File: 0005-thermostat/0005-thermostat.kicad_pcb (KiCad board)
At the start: 2 copper layers, 41 parts, among them J1 EXT_NTC, J2 OUT, J3 PWR, J4 EXT_LED, J5 EXT_P1, J6 EXT_P2, P1 22k, P2 22k, T1 BC847B, T2 BC847B, T3 BC847B

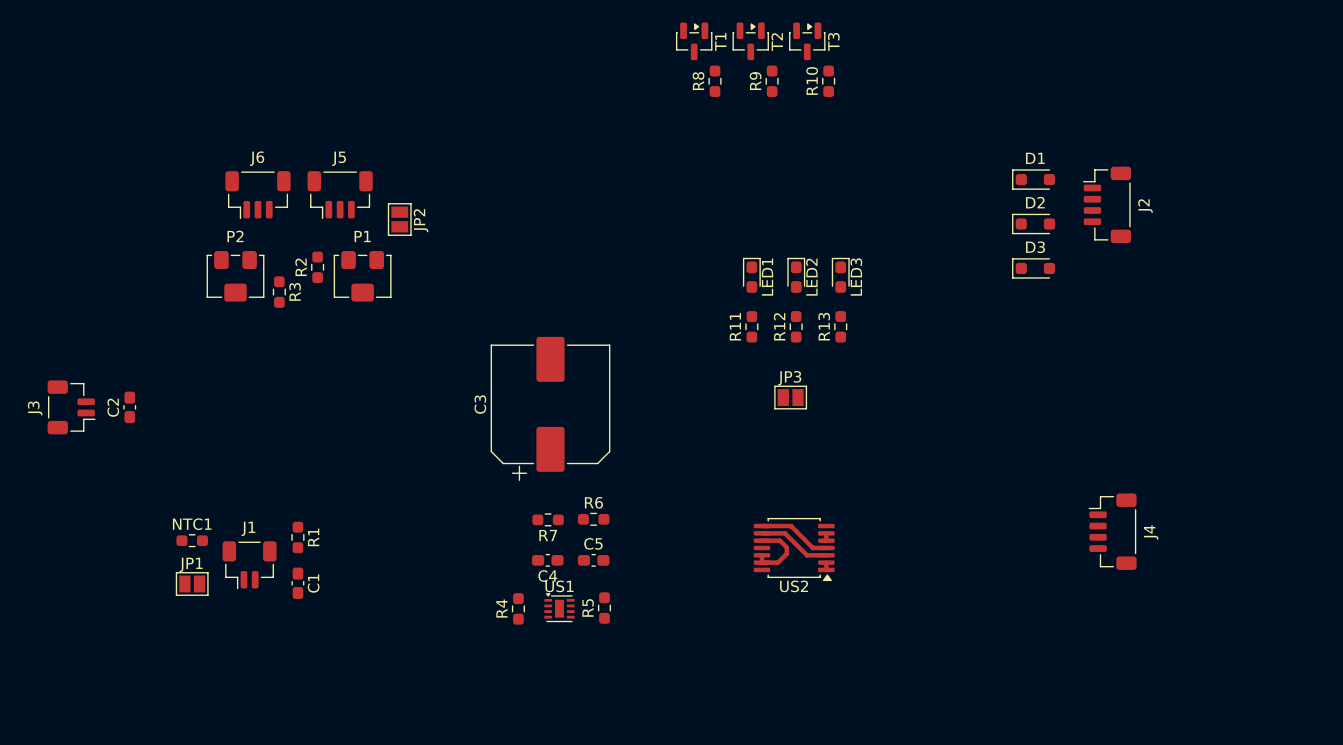
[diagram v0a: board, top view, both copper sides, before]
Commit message: PCB - new sections designed
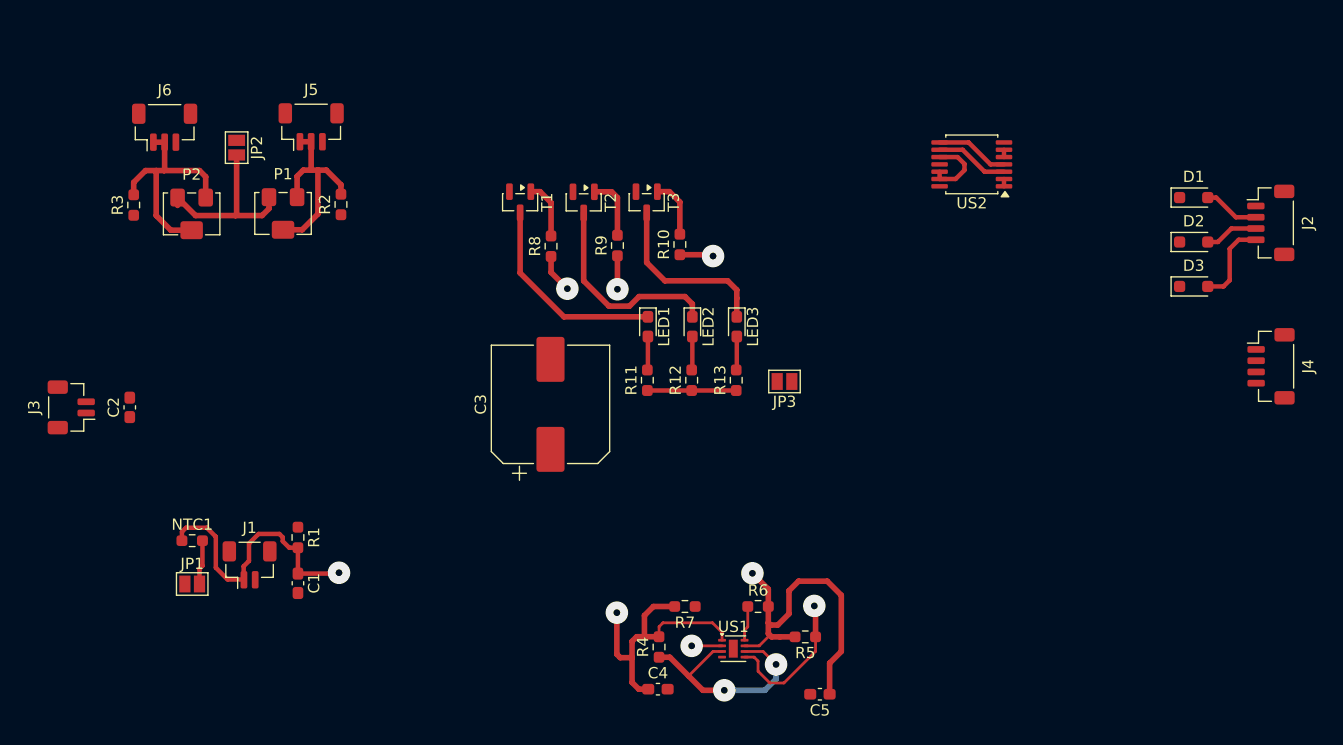
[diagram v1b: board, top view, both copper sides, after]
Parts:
- moved US2 37.6 mm to (177.2, 75.0)
- moved C5 23.4 mm to (163.7, 122.1), turned to 180 degrees
- moved T1 21.1 mm to (137.0, 78.4)
- moved R8 20.7 mm to (139.8, 82.3)
- moved T2 20.6 mm to (142.7, 78.4)
- moved J4 20.3 mm to (203.8, 93.0)
- moved T3 20.2 mm to (148.2, 78.4)
- moved R9 20.1 mm to (145.7, 82.2)
- moved R10 19.6 mm to (151.2, 82.1)
- moved R5 18.0 mm to (162.3, 117.0), turned to 180 degrees
- moved R6 16.5 mm to (158.2, 114.3)
- moved US1 15.9 mm to (155.9, 118.0)
- moved JP2 15.8 mm to (111.8, 73.5)
- moved R3 15.1 mm to (102.7, 78.6), turned to 90 degrees
- moved C4 15.1 mm to (149.2, 121.7), turned to 0 degrees
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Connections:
- J4 pad MP: (no net) -> GNDD
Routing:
- net Net-(J1-Pin_1): track 0.00 -> 45.3 mm, vias 0 -> 3
- net Net-(C5-Pad1): track 0.65 -> 34.3 mm, vias 0 -> 2
- net Net-(J5-Pin_1): track 0.00 -> 31.5 mm, vias 0 -> 1
- net Net-(C4-Pad1): track 0.65 -> 29.3 mm, vias 0 -> 2
- net Net-(J6-Pin_1): track 0.00 -> 23.9 mm, vias 0 -> 1
- net Net-(D3-A): track 0.00 -> 23.0 mm
- net Net-(D1-A): track 0.00 -> 22.9 mm
- net Net-(D2-A): track 0.00 -> 22.7 mm
- net Net-(JP2-B): track 0.00 -> 16.2 mm
- net Net-(JP3-B): track 0.00 -> 7.90 mm
- net Net-(T2-B): track 0.00 -> 5.61 mm
- net Net-(T3-B): track 0.00 -> 5.24 mm
- net Net-(T1-B): track 0.00 -> 5.17 mm
- net Net-(JP1-B): track 0.00 -> 3.96 mm
- net +12V: track 0.00 -> 3.12 mm
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
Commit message: PCB design - connecting modules
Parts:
- moved J3 47.7 mm to (143.8, 106.2), turned to -90 degrees
- moved C2 37.5 mm to (138.6, 106.2), turned to -90 degrees
- moved R3 34.2 mm to (131.6, 96.9)
- moved D3 32.2 mm to (165.7, 93.7)
- moved D1 32.2 mm to (165.7, 85.8)
- moved D2 32.2 mm to (165.7, 89.7)
- moved J2 32.2 mm to (172.5, 88.0)
- moved J4 32.2 mm to (172.5, 100.8)
- moved J6 28.2 mm to (121.2, 95.0), turned to 90 degrees
- moved P2 24.1 mm to (128.7, 91.4), turned to 90 degrees
- moved JP2 19.0 mm to (122.8, 89.1), turned to 0 degrees
- moved NTC1 18.4 mm to (124.3, 100.2), turned to 180 degrees
- moved US2 18.2 mm to (159.8, 80.5), turned to -90 degrees
- moved R1 15.7 mm to (131.7, 102.0)
- moved R2 15.4 mm to (133.7, 87.4)
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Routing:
- net Net-(D2-A): track 22.7 -> 153.5 mm, vias 0 -> 3
- net Net-(D1-A): track 22.9 -> 133.7 mm, vias 0 -> 3
- net Net-(J5-Pin_1): track 31.5 -> 101.3 mm, vias 1 -> 2
- net Net-(D3-A): track 23.0 -> 85.4 mm, vias 0 -> 3
- net Net-(C5-Pad1): track 34.3 -> 83.8 mm, vias 2 -> 3
- net Net-(C4-Pad1): track 29.3 -> 75.1 mm, vias 2 -> 3
- net Net-(J6-Pin_1): track 23.9 -> 59.3 mm, vias 1 -> 2
- net Net-(R9-Pad1): track 2.97 -> 24.2 mm, vias 1 -> 2
- net Net-(J1-Pin_1): track 45.3 -> 61.8 mm
- net Net-(JP3-B): track 7.90 -> 11.9 mm
- net Net-(JP2-B): track 16.2 -> 17.8 mm
- net Net-(JP1-B): track 3.96 -> 5.40 mm

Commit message: PCB finished
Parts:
- added REF**: MountingHole_3.2mm_M3_DIN965_Pad, MountingHole:MountingHole_3.2mm_M3_DIN965_Pad, F.Cu at (177.6, 108.2)
- added REF**: TestPoint_THTPad_D2.0mm_Drill1.0mm, TestPoint:TestPoint_THTPad_D2.0mm_Drill1.0mm, F.Cu at (117.7, 89.2)
- added REF**: TestPoint_THTPad_D2.0mm_Drill1.0mm, TestPoint:TestPoint_THTPad_D2.0mm_Drill1.0mm, F.Cu at (170.5, 74.8)
- added REF**: MountingHole_3.2mm_M3_DIN965_Pad, MountingHole:MountingHole_3.2mm_M3_DIN965_Pad, F.Cu at (119.0, 75.8)
- added REF**: MountingHole_3.2mm_M3_DIN965_Pad, MountingHole:MountingHole_3.2mm_M3_DIN965_Pad, F.Cu at (119.0, 108.2)
- added REF**: TestPoint_THTPad_D2.0mm_Drill1.0mm, TestPoint:TestPoint_THTPad_D2.0mm_Drill1.0mm, F.Cu at (172.0, 110.0)
- added REF**: TestPoint_THTPad_D2.0mm_Drill1.0mm, TestPoint:TestPoint_THTPad_D2.0mm_Drill1.0mm, F.Cu at (178.8, 82.5)
- added REF**: TestPoint_THTPad_D2.0mm_Drill1.0mm, TestPoint:TestPoint_THTPad_D2.0mm_Drill1.0mm, F.Cu at (124.8, 73.8)
- added REF**: MountingHole_3.2mm_M3_DIN965_Pad, MountingHole:MountingHole_3.2mm_M3_DIN965_Pad, F.Cu at (177.6, 75.8)
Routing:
- net +12V: track 3.12 -> 154.6 mm
- net Net-(J5-Pin_1): track 101.3 -> 107.3 mm
- net GNDD: track 0.00 -> 5.87 mm
- net Net-(D1-A): track 133.7 -> 136.3 mm
- net Net-(D3-A): track 85.4 -> 88.0 mm
- net Net-(C4-Pad1): track 75.1 -> 77.3 mm
- net Net-(C5-Pad1): track 83.8 -> 85.7 mm
- net Net-(US2-Pad10): track 6.20 -> 4.63 mm
- net Net-(D2-A): track 153.5 -> 154.8 mm
- net Net-(J6-Pin_1): track 59.3 -> 60.2 mm
- added copper zone on B.Cu, net GNDD
- added copper zone on F.Cu, net GNDD
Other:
- board outline added: 68.5 x 42 mm
- board text added: "${GH_REPO}"
- board text added: "${GH_REPO} REV ${VERSION}"
- board text added: "REV ${VERSION}"

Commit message: PCB update
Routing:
- net +12V: track 154.6 -> 121.7 mm
- net Net-(D2-A): track 154.8 -> 166.8 mm
- net Net-(J5-Pin_1): track 107.3 -> 95.5 mm
- net Net-(JP3-B): track 11.9 -> 19.8 mm
- net Net-(LED1-A): track 2.62 -> 7.38 mm
- net Net-(LED3-A): track 2.62 -> 7.34 mm
- net Net-(C4-Pad1): track 77.3 -> 73.5 mm
- net Net-(JP2-B): track 17.8 -> 21.2 mm
- net Net-(J6-Pin_1): track 60.2 -> 56.8 mm
- net GNDD: track 5.87 -> 4.38 mm
- net Net-(D1-A): track 136.3 -> 137.5 mm
- net Net-(R9-Pad1): track 24.2 -> 23.4 mm

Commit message: Update PCB
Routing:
- net Net-(C5-Pad1): track 85.5 -> 87.7 mm
- net Net-(J5-Pin_1): track 95.5 -> 97.2 mm
- net Net-(D3-A): track 88.2 -> 87.4 mm
- net Net-(D1-A): track 137.5 -> 137.0 mm
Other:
- board text removed: "${GH_REPO} REV ${VERSION}"

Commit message: Update PCB
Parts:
- moved D3 1.03 mm to (165.6, 92.6)
- moved D1 0.97 mm to (165.6, 86.7)
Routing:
- net Net-(D1-A): track 137.0 -> 145.0 mm
- net +12V: track 121.7 -> 114.4 mm
- net Net-(D3-A): track 87.4 -> 86.6 mm
